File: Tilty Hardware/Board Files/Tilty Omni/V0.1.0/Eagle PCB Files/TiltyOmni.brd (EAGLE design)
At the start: 41.9 x 52.1 mm, 38 parts, among them U1 TEENSY_3.0_ALLPINSTEENSY_3.0_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, U2 HC-09_BREAKOUT, U4 LM2931, U5 MPU-6050, U7 SPI_FLASH-X25XXSMD

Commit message: Still working on the Tilty Omni...
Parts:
- moved JP2 1.27 mm to (4.45, 21.5)
- moved JP3 1.27 mm to (37.5, 21.5)
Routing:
- net A12: track 0.00 -> 44.3 mm, vias 0 -> 1
- net 31: track 0.00 -> 38.3 mm, vias 0 -> 3
- net 32: track 0.00 -> 37.0 mm, vias 0 -> 1
- net A10: track 0.00 -> 36.7 mm, vias 0 -> 1
- net A11: track 0.00 -> 36.5 mm, vias 0 -> 1
- net BT_CMD: track 0.00 -> 36.0 mm, vias 0 -> 1
- net 26: track 0.00 -> 35.3 mm, vias 0 -> 1
- net 24: track 0.00 -> 34.6 mm, vias 0 -> 1
- net 25: track 0.00 -> 34.3 mm, vias 0 -> 1
- net 30: track 0.00 -> 33.3 mm, vias 0 -> 3
- net 29: track 0.00 -> 32.1 mm, vias 0 -> 1
- net GND: track 55.4 -> 84.3 mm, vias 3 -> 5
- net MEMORY_CS: track 19.0 -> 35.2 mm, vias 2 -> 3
- net BATT_SENSE: track 24.9 -> 40.5 mm
- net SCK: track 41.4 -> 35.8 mm
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
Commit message: Tilty omni work
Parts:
- moved D4 0.51 mm to (35.6, 44.5)
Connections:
- net 5V_SCL: no longer JP7.11
- net 5V_SDA: now also JP7.11
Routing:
- net +5V: track 8.53 -> 71.4 mm, vias 0 -> 4
- net +3V3: track 71.4 -> 118.9 mm, vias 7 -> 11
- net 20/A6: track 0.00 -> 15.6 mm
- net SERVO_3: track 0.00 -> 14.9 mm
- net SERVO_4: track 0.00 -> 14.8 mm
- net AGND: track 0.00 -> 14.6 mm
- net 21/A7: track 0.00 -> 14.3 mm
- net N$4: track 0.00 -> 13.4 mm
- net 3V_SCL: track 15.9 -> 25.2 mm
- net 3V_SDA: track 13.2 -> 22.6 mm, vias 1 -> 3
- net 5V_SDA: track 10.4 -> 15.6 mm
- net 5V_SCL: track 10.5 -> 15.6 mm
- net 15/A1: track 11.7 -> 16.8 mm
- net 14/A0: track 10.5 -> 15.5 mm
- net A10: track 36.7 -> 36.0 mm
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
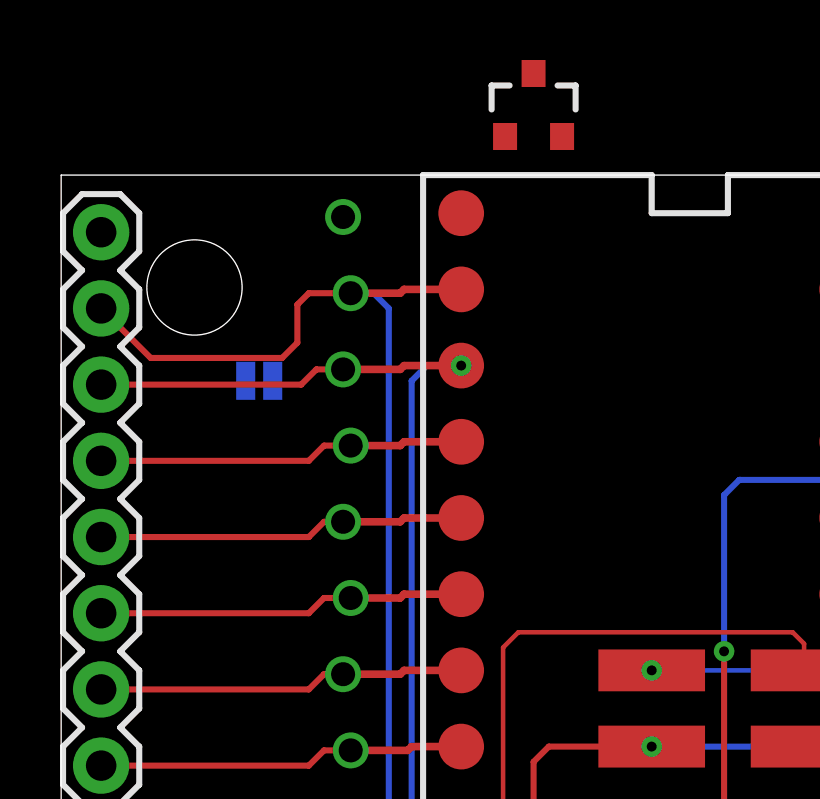
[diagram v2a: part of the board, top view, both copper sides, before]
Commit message: Updated Tilty Duo/Quad Things.todo and moved a couple parts on Tilty Omni
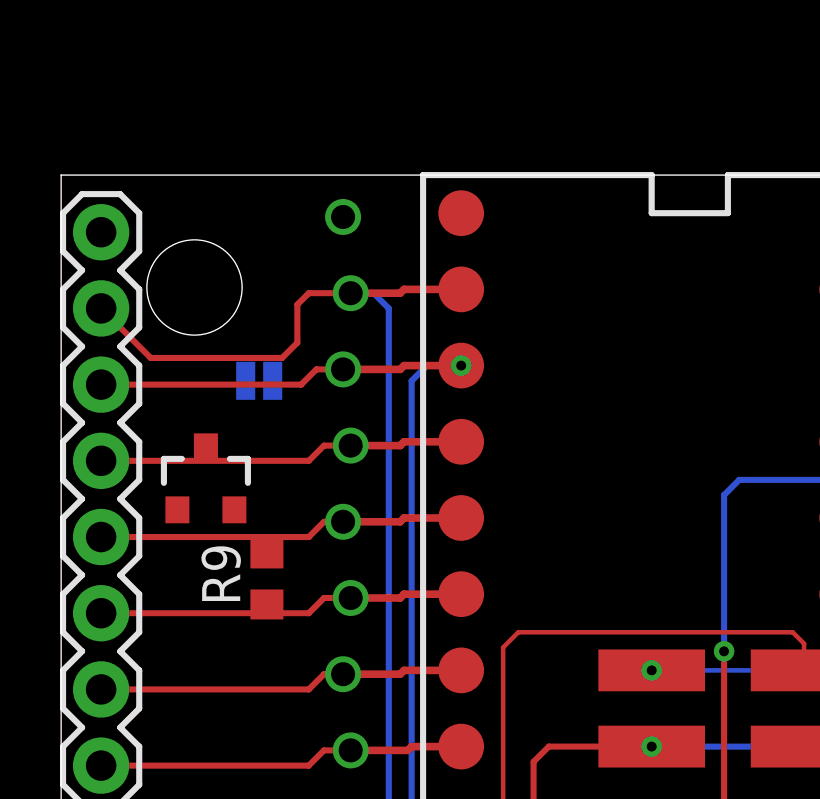
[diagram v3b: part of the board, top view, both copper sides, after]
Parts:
- added R9: (no value), resistor:R0603
- moved D5 16.6 mm to (4.83, 41.9)
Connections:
- new net N$5: D5.1, R9.2
- net GND: now also R9.1; no longer D5.1
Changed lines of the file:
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@@
 <attribute name="VALUE" x="34.544" y="44.2595" size="0.4064" layer="27"/>
 </element>
-<element name="D5" library="SparkFun-DiscreteSemi" package="SOT23-3" value="" x="15.748" y="54.356" smashed="yes">
-<attribute name="PART#" value="BZX84C3V3LT1GOSCT-ND" x="70.358" y="-26.924" size="1.778" layer="27" display="off"/>
-<attribute name="VALUE" x="14.732" y="54.1655" size="0.4064" layer="27"/>
+<element name="D5" library="SparkFun-DiscreteSemi" package="SOT23-3" value="" x="4.826" y="41.91" smashed="yes">
+<attribute name="PART#" value="BZX84C3V3LT1GOSCT-ND" x="59.436" y="-39.37" size="1.778" layer="27" display="off"/>
+<attribute name="VALUE" x="3.81" y="41.7195" size="0.4064" layer="27"/>
 </element>
 <element name="U1" library="Teensy3.0" package="TEENSY_3.0_ALLPINS-SMD" value="TEENSY_3.0_ALLPINSTEENSY_3.0_ALLPINS-SMD" x="20.955" y="34.29" smashed="yes"/>
@@
 <element name="JP6" library="SparkFun-Connectors" package="1X20" value="M20" x="1.3335" y="1.905" smashed="yes" rot="R90"/>
 <element name="JP7" library="SparkFun-Connectors" package="1X20" value="M20" x="40.5765" y="1.905" smashed="yes" rot="R90"/>
+<element name="R9" library="resistor" package="R0603" value="" x="6.858" y="38.608" rot="R90"/>
 </elements>
 <signals>
@@
 <contactref element="U7" pad="4"/>
 <contactref element="C13" pad="1"/>
-<contactref element="D5" pad="1"/>
 <contactref element="JP2" pad="P$8"/>
 <contactref element="JP3" pad="P$8"/>
@@
 <wire x1="29.972" y1="25.4" x2="31" y2="25.4" width="0.2032" layer="1"/>
 <wire x1="31" y1="25.4" x2="31.02" y2="25.38" width="0.2032" layer="1"/>
+<contactref element="R9" pad="1"/>
 <wire x1="25.8445" y1="33.02" x2="32.512" y2="48.133" width="0" layer="19" extent="16-16"/>
 <wire x1="35.394" y1="12.7" x2="35.472" y2="18.2" width="0" layer="19" extent="1-1"/>
@@
 <wire x1="1.3335" y1="50.165" x2="6.154" y2="45.212" width="0" layer="19" extent="16-16"/>
 <wire x1="13.335" y1="50.8" x2="6.154" y2="45.212" width="0" layer="19" extent="1-16"/>
-<wire x1="14.798" y1="53.356" x2="13.335" y2="50.8" width="0" layer="19" extent="1-1"/>
+<wire x1="6.858" y1="37.758" x2="4.572" y2="12.573" width="0" layer="19" extent="1-1"/>
 </signal>
 <signal name="AGND">
@@
 <wire x1="37.338" y1="34.29" x2="33.274" y2="34.29" width="0.2032" layer="16"/>
 <wire x1="37.846" y1="35.306" x2="37.846" y2="37.846" width="0.2032" layer="1"/>
-<wire x1="9.398" y1="50.673" x2="15.748" y2="55.456" width="0" layer="19" extent="1-1"/>
-<wire x1="28.575" y1="45.72" x2="15.748" y2="55.456" width="0" layer="19" extent="1-1"/>
+<wire x1="9.398" y1="50.673" x2="4.826" y2="43.01" width="0" layer="19" extent="1-1"/>
+<wire x1="28.575" y1="45.72" x2="4.826" y2="43.01" width="0" layer="19" extent="1-1"/>
 </signal>
 <signal name="+5V">
@@
 <wire x1="8.255" y1="32.385" x2="1.3335" y2="32.385" width="0.2032" layer="1"/>
 </signal>
+<signal name="N$5">
+<contactref element="D5" pad="1"/>
+<contactref element="R9" pad="2"/>
+<wire x1="6.858" y1="39.458" x2="3.876" y2="40.91" width="0" layer="19" extent="1-1"/>
+</signal>
 </signals>

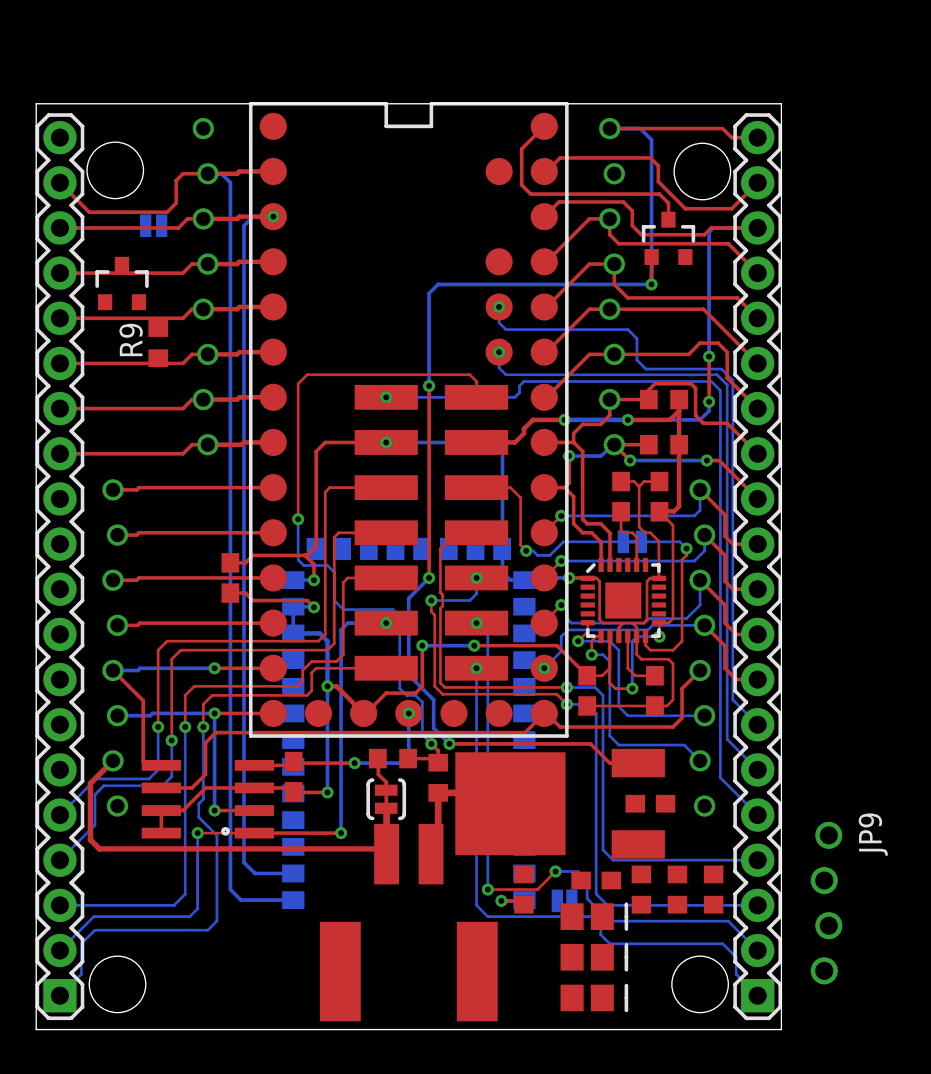
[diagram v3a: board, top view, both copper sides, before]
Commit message: Finished preliminary Tilty Omni design!
Still needs review before being ordered
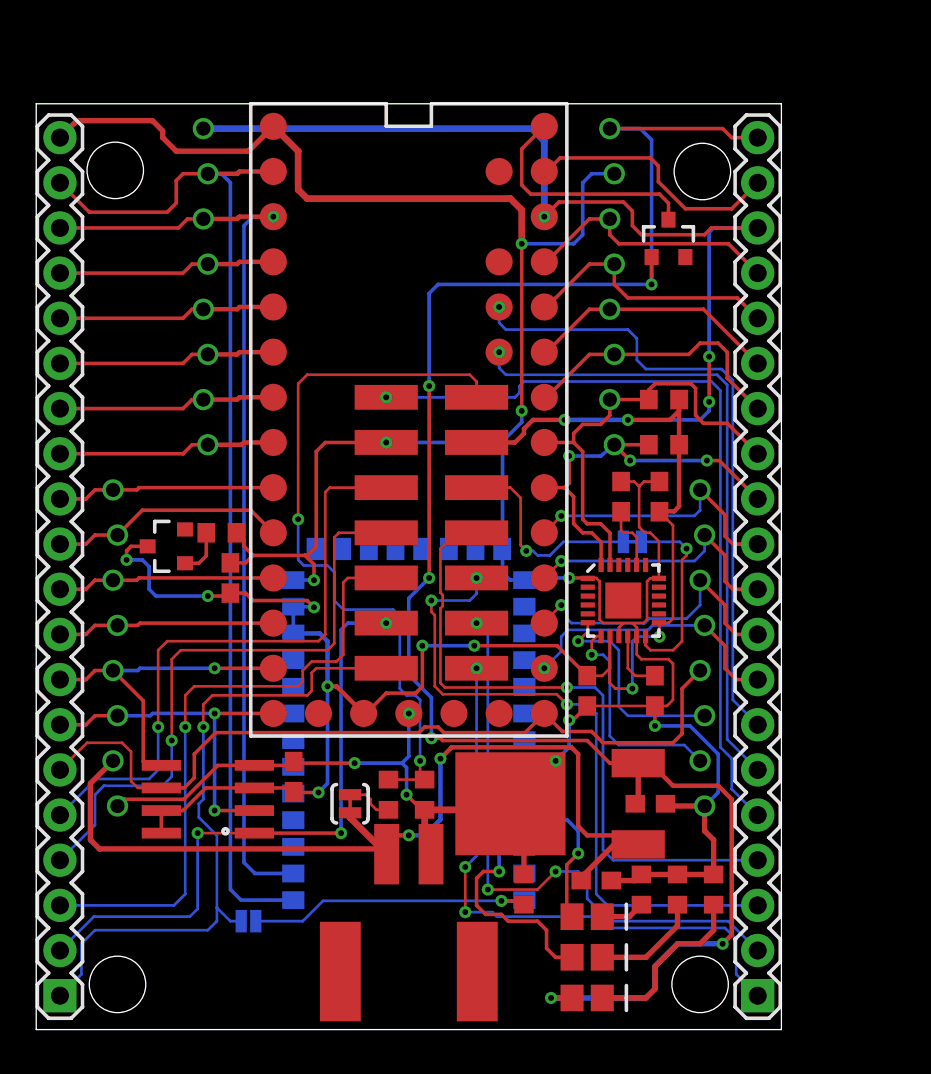
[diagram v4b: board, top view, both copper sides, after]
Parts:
- removed JP9: (no value), pinhead:1X04_NO_SS_LOCKING
- removed SJ1: SOLDERJUMPERNO, SparkFun-Passives:SJ_2S-NO
- moved SJ5 17.8 mm to (11.9, 6.10), turned to 180 degrees
- moved D5 14.9 mm to (7.37, 27.2), turned to 90 degrees
- moved R9 11.2 mm to (10.4, 27.9), turned to 180 degrees
- moved SJ4 2.05 mm to (17.7, 12.7)
- moved R5 2.05 mm to (19.8, 13.2), turned to 90 degrees
- moved R6 1.22 mm to (21.8, 13.2)
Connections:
- removed net CHASSIS_GND: SJ1.1
- removed net RX1: JP9.2
- removed net TX1: JP9.1
- net +5V: no longer JP9.4
- net GND: no longer JP9.3, SJ1.2
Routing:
- net GND: track 84.3 -> 184.4 mm, vias 5 -> 11
- net +3V3: track 118.9 -> 151.7 mm, vias 11 -> 14
- net +5V: track 71.4 -> 101.4 mm, vias 4 -> 6
- net VCC: track 24.6 -> 53.1 mm, vias 0 -> 2
- net CMD: track 2.67 -> 17.0 mm
- net YEL_LED: track 0.00 -> 12.8 mm, vias 0 -> 1
- net N$13: track 0.00 -> 10.0 mm
- net SCK: track 35.8 -> 45.5 mm
- net N$14: track 0.00 -> 8.66 mm, vias 0 -> 1
- net N$24: track 0.00 -> 6.15 mm
- net 8/TX3: track 8.82 -> 13.3 mm
- net MISO: track 16.5 -> 20.0 mm
- net 10/TX2: track 8.82 -> 12.3 mm
- net 7/RX3: track 9.07 -> 12.3 mm
- net MOSI: track 16.0 -> 19.2 mm
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
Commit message: Made final revisions to Tilty Omni and R/C Receiver adapter before ordering!
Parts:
- moved MPU_INT 9.16 mm to (24.9, 30.5), turned to 0 degrees
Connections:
- removed net VUSB: U1.VUSB
- net +5V: now also U1.VUSB
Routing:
- net +5V: track 101.4 -> 115.0 mm, vias 6 -> 7
- net N$16: track 10.9 -> 22.7 mm
- net IMU_INT: track 11.7 -> 4.32 mm
- net GND: track 184.4 -> 190.6 mm
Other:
- board text added: "+"
- board text added: "-"
- board text added: "0"
- board text added: "1"
- board text added: "10"
- board text added: "11"
- board text added: "12"
- board text added: "14/13"
- board text added: "15/12"
- board text added: "16/15"
- board text added: "17/16"
- board text added: "18"
- board text added: "18/17"
- board text added: "19"
- board text added: "2"
- board text added: "20"
- board text added: "21"
- board text added: "22"
- board text added: "23"
- board text added: "25"
- board text added: "26"
- board text added: "27"
- board text added: "28"
- board text added: "29"
- board text added: "3"
- board text added: "30"
- board text added: "31"
- board text added: "32"
- board text added: "3v3"
- board text added: "4"
- board text added: "5"
- board text added: "5v"
- board text added: "6"
- board text added: "7"
- board text added: "8"
- board text added: "9"
- board text added: "A10/ADA"
- board text added: "A11/ACL"
- board text added: "A12/GND"
- board text added: "BT"
- board text added: "CMD"
- board text added: "GND"
- board text added: "IMU"
- board text added: "INT"
- board text added: "P"
- board text added: "SJ1"
- board text added: "Tilty Omni"
- board text added: "Vin"
- board text added: "v0.1.0"
